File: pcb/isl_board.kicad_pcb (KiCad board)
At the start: 2 copper layers, 82.3 x 75 mm, 98 parts, among them J1 CONN_02X20, J2 SMA_PCLK, J3 SMA_PCLK_SI, J4 SCART-F, J5 CONN_01X02, U1 AP7351C, U2 TLV70033DDC, U3 NCP703SN18T1G, U4 TLV70018, U5 ISL51002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

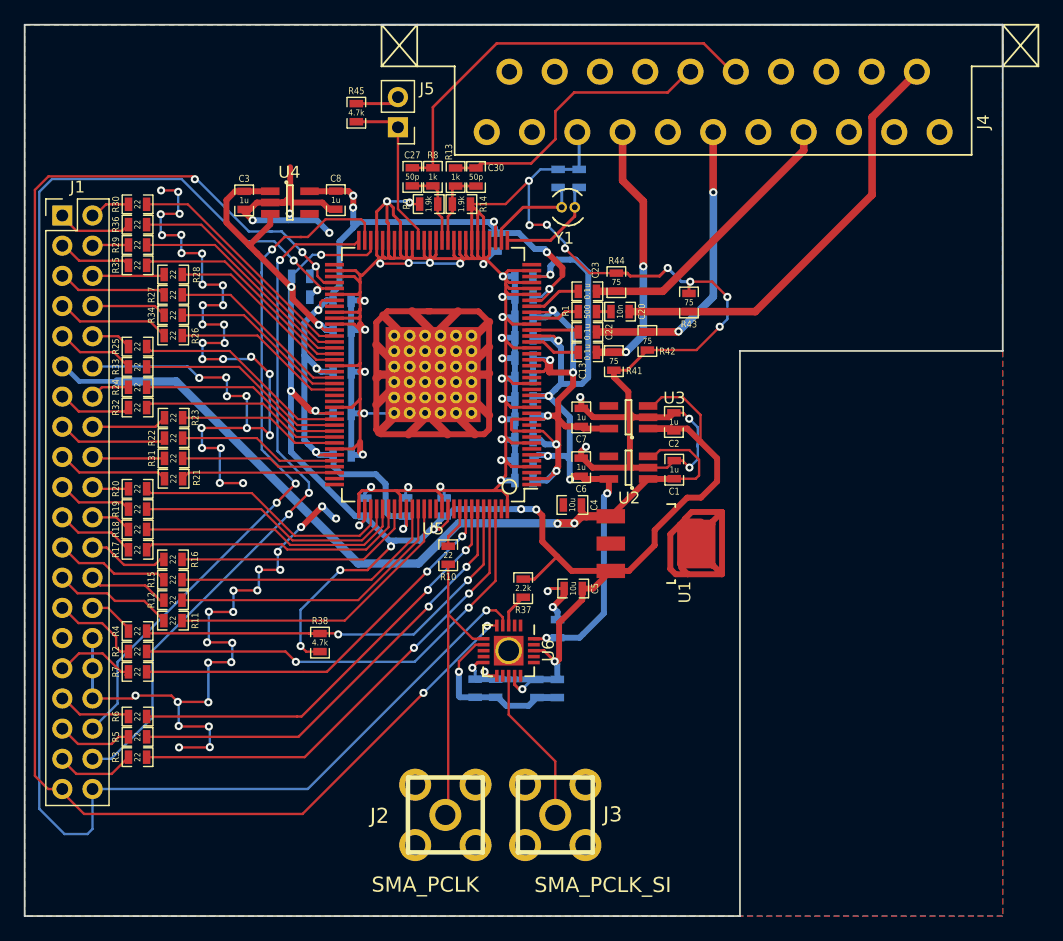
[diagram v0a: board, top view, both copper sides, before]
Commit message: update PCB to v1.1
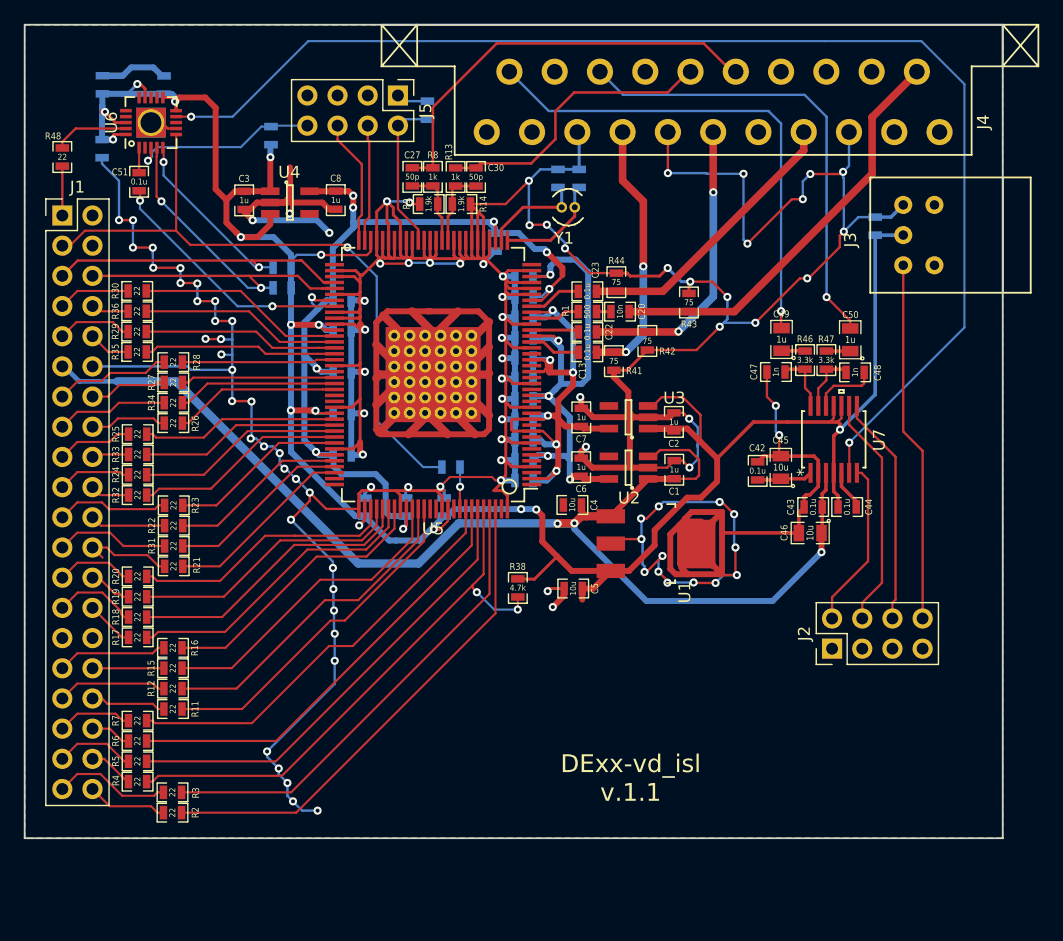
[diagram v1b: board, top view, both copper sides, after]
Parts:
- removed C39, C40: 0.1u, custom_components:SM0603_Capa_libcms
- added C42: 0.1u, custom_components:SM0603_Capa_libcms, F.Cu at (79.1, 64.1)
- added C43: 0.1u, custom_components:SM0603_Capa_libcms, F.Cu at (83.8, 67.1)
- added C44: 0.1u, custom_components:SM0603_Capa_libcms, F.Cu at (86.7, 67.1)
- added C45: 10u, custom_components:SM0805_libcms, F.Cu at (81.1, 63.8)
- added C46: 10u, custom_components:SM0805_libcms, F.Cu at (83.6, 69.3)
- added C47: 1n, custom_components:SM0603_Capa_libcms, F.Cu at (80.7, 55.8)
- added C48: 1n, custom_components:SM0603_Capa_libcms, F.Cu at (87.3, 55.8)
- added C49: 1u, custom_components:SM0805_libcms, F.Cu at (81.2, 53.0)
- added C50: 1u, custom_components:SM0805_libcms, F.Cu at (86.9, 53.1)
- added C51: 0.1u, custom_components:SM0603_Capa_libcms, F.Cu at (27.1, 39.8)
- added C52: 0.1u, custom_components:SM0603_Capa_libcms, B.Cu at (89.0, 43.5)
- added R46: 3.3k, custom_components:SM0603_Resistor_libcms, F.Cu at (83.1, 54.8)
- added R47: 3.3k, custom_components:SM0603_Resistor_libcms, F.Cu at (84.9, 54.8)
- added R48: 22, custom_components:SM0603_Resistor_libcms, F.Cu at (20.6, 37.7)
- added U7: PCM1808PWR, custom_components:PCM1808PWR, F.Cu at (85.5, 61.4)
- J2: value SMA_PCLK -> CONN_AUD; footprint custom_components:SMA_CONN -> Connector_PinHeader_2.54mm:PinHeader_2x04_P2.54mm_Vertical
- J3: value SMA_PCLK_SI -> EAPLRAA4; footprint custom_components:SMA_CONN -> custom_components:EAPLRAA4
- J5: value CONN_01X02 -> CONN_02X04; footprint Pin_Headers:Pin_Header_Straight_1x02_Pitch2.54mm -> Connector_PinHeader_2.54mm:PinHeader_2x04_P2.54mm_Vertical
- R10, R37, R45: moved to B.Cu
- moved C38 63.6 mm to (24.0, 31.6), turned to 90 degrees
- moved C41 57.9 mm to (29.2, 31.6), turned to 90 degrees
- moved J3 56.9 mm to (91.4, 44.2), turned to 270 degrees
- moved C37 55.7 mm to (24.0, 37.0), turned to 270 degrees
- moved U6 53.7 mm to (28.1, 34.8), turned to 90 degrees
- moved R37 43.6 mm to (38.2, 35.9), turned to 270 degrees
- moved J2 35.4 mm to (85.4, 79.0), turned to 90 degrees
- moved R38 17.3 mm to (59.0, 73.9), turned to 90 degrees
- moved R2 13.9 mm to (29.9, 92.8)
- moved R4 12.7 mm to (27.0, 90.2)
- moved R11 7.44 mm to (29.9, 84.1)
- moved R12 7.44 mm to (29.9, 82.4)
- moved R15 7.44 mm to (29.9, 80.7)
- moved R16 7.44 mm to (29.9, 79.0)
- moved R10 7.42 mm to (53.3, 63.8), turned to 0 degrees
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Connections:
- C37 pad 1: /AVCC3v3 -> /DVDD3v3
- J1 pad 1: /B[6] -> /PCLK_SI
- J1 pad 10: /G[7] -> /B[4]
- J1 pad 13: /G[4] -> /B[3]
- J1 pad 14: /G[5] -> /B[2]
- J1 pad 15: /G[2] -> /B[1]
- J1 pad 16: /G[3] -> /B[0]
- J1 pad 17: /G[0] -> /G[7]
- J1 pad 18: /G[1] -> /G[6]
- J1 pad 19: /R[6] -> /G[5]
- J1 pad 2: /B[7] -> GND
- J1 pad 20: /R[7] -> /G[4]
- J1 pad 21: /R[4] -> /G[3]
- J1 pad 22: /R[5] -> /G[2]
- J1 pad 23: /R[2] -> /G[1]
- J1 pad 24: /R[3] -> /G[0]
- J1 pad 25: /R[0] -> /R[7]
- J1 pad 26: /R[1] -> /R[6]
- J1 pad 27: /FID -> /R[5]
- J1 pad 28: /INT_N -> /R[4]
- J1 pad 3: /B[4] -> /PCLK
- J1 pad 31: /HS -> /R[3]
- J1 pad 32: GND -> /R[2]
- J1 pad 33: /HSYNC -> /R[1]
- J1 pad 34: GND -> /R[0]
- J1 pad 35: /VSYNC -> /HS
- J1 pad 36: /CLAMP -> /HSYNC
- J1 pad 37: /DE -> /VSYNC
- J1 pad 38: /COAST -> /INT_N
- J1 pad 39: /SDA -> /DE
- J1 pad 4: /B[5] -> GND
- J1 pad 40: /SCL -> /FID
- J1 pad 5: /B[2] -> /SDA
- J1 pad 6: /B[3] -> /SCL
- J1 pad 7: /B[0] -> /B[7]
- J1 pad 8: /B[1] -> /B[6]
- J1 pad 9: /G[6] -> /B[5]
- J2 pad 1: /PCLK -> GND
- J2 pad 2: GND -> /I2S_WS
- J3 pad 1: /PCLK_SI -> GND
- J3 pad 2: GND -> /DVDD3v3
- J4 pad 2: Net-(J4-Pad2) -> /AUD_R
- J4 pad 6: Net-(J4-Pad6) -> /AUD_L
- J5 pad 1: Net-(J5-Pad1) -> GND
- J5 pad 2: GND -> Net-(J5-Pad2)
- R37 pad 1: /INTR -> /SI_INT_N
- R45 pad 2: Net-(J5-Pad1) -> Net-(J5-Pad2)
- U2 pad 4: (no net) -> Net-(U2-Pad4)
- U3 pad 4: (no net) -> Net-(U3-Pad4)
- U4 pad 4: (no net) -> Net-(U4-Pad4)
- U5 pad 54: Net-(J5-Pad1) -> Net-(J5-Pad2)
- U6 pad 13: /PCLK_SI -> Net-(U6-Pad13)
- U6 pad 20: /AVCC3v3 -> /DVDD3v3
- U6 pad 3: /INTR -> /SI_INT_N
- U6 pad 9: Net-(U6-Pad9) -> /PCM_MCLK
- U6 pad EP: (no net) -> GND
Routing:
- net /PCM_MCLK: track 0.00 -> 107.2 mm, vias 0 -> 2
- net /SCL: track 133.5 -> 40.2 mm, vias 3 -> 2
- net GND: track 637.2 -> 727.2 mm, vias 96 -> 102
- net /SDA: track 128.5 -> 41.0 mm, vias 5 -> 2
- net /CLAMP: track 59.6 -> 9.86 mm, vias 3 -> 0
- net /COAST: track 58.9 -> 10.6 mm, vias 3 -> 0
- net /AUD_R: track 0.00 -> 41.9 mm, vias 0 -> 1
- net /DVDD3v3: track 177.0 -> 218.2 mm
- net /AUD_L: track 0.00 -> 39.3 mm, vias 0 -> 1
- net /DVDD5: track 72.3 -> 104.6 mm, vias 2 -> 3
- net /PCLK: track 25.2 -> 56.1 mm, vias 0 -> 1
- net /SPDIF: track 0.00 -> 30.4 mm
- net Net-(C51-Pad1): track 0.00 -> 21.3 mm, vias 0 -> 2
- net /I2S_DATA: track 0.00 -> 19.7 mm
- net /I2S_BCK: track 0.00 -> 19.3 mm
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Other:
- board size 82.3 x 75 mm -> 82.3 x 68.5 mm
- rule pad_to_mask_clearance: 0.2 -> 0.0508
- board text added: "DExx-vd_isl v.1.1"

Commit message: update PCB to v1.2
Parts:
- added C39: 0.1u, custom_components:SM0603_Capa_libcms, F.Cu at (83.9, 90.9)
- added C53: 0.1u, custom_components:SM0603_Capa_libcms, B.Cu at (32.5, 30.4)
- added DS1: NHD-0220CW-AW3, Connector_PinHeader_2.54mm:PinHeader_1x20_P2.54mm_Vertical, F.Cu at (87.6, 93.7)
- added R49: 10k, custom_components:SM0603_Resistor_libcms, F.Cu at (49.5, 90.4)
- added R50: 10k, custom_components:SM0603_Resistor_libcms, F.Cu at (44.4, 90.4)
- added R51: 1k, custom_components:SM0603_Resistor_libcms, F.Cu at (25.1, 39.8)
- added U8: TSOP31338, OptoDevice:Vishay_CAST-3Pin, F.Cu at (31.3, 28.2)
- C13, C22, C23: value 0.1u -> 1n
- R3: value 22 -> 2.2k
- Y1: value 27MHz -> 24.576MHz
- moved R3 49.1 mm to (26.5, 42.1), turned to 180 degrees
- moved J2 5.83 mm to (79.9, 77.0)
- moved C52 2.48 mm to (89.0, 46.0)
- moved R2 1.67 mm to (29.9, 91.2)
- moved R38 1.57 mm to (59.1, 72.4)
- moved R45 1.11 mm to (52.5, 33.7)
- moved J5 1.03 mm to (49.9, 32.5)
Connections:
- J1 pad 39: /DE -> /IR_RX
- J3 pad 1: GND -> /SPDIF
- J3 pad 2: /DVDD3v3 -> GND
- J3 pad 3: /SPDIF -> /DVDD3v3
- R3 pad 1: /DE -> /CLK24P576
- R3 pad 2: Net-(R3-Pad2) -> Net-(C51-Pad1)
- U5 pad 125: Net-(R3-Pad2) -> Net-(U5-Pad125)
- U5 pad 72: Net-(C51-Pad1) -> /CLK24P576
- U6 pad 9: /PCM_MCLK -> Net-(U6-Pad9)
- U7 pad 6: /PCM_MCLK -> /CLK24P576
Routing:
- net /CLK24P576: track 0.00 -> 133.2 mm, vias 0 -> 3
- net /PCM_MCLK: track 107.2 -> 0.00 mm, vias 2 -> 0
- net /DVDD3v3: track 218.2 -> 320.9 mm, vias 16 -> 18
- net /SCL: track 40.2 -> 122.1 mm
- net /SDA: track 41.0 -> 121.6 mm
- net /IR_RX: track 0.00 -> 80.4 mm
- net GND: track 727.2 -> 798.2 mm, vias 102 -> 105
- net Net-(R3-Pad2): track 40.0 -> 0.00 mm
- net Net-(C51-Pad1): track 21.3 -> 3.70 mm, vias 2 -> 0
- net /DE: track 9.91 -> 0.00 mm
- net /SPDIF: track 30.4 -> 35.0 mm
- net /SI_INT_N: track 16.0 -> 19.4 mm, vias 1 -> 2
- net Net-(DS1-Pad18): track 0.00 -> 2.55 mm
- net Net-(DS1-Pad16): track 0.00 -> 2.53 mm
- net Net-(R2-Pad2): track 42.2 -> 40.0 mm
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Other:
- outline, holes or cut-outs redrawn
- board text added: "DExx-vd_isl v.1.2"
- board text removed: "DExx-vd_isl v.1.1"

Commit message: update PCB to v1.3
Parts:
- added L1: 2.2u, custom_components:CDRH2D14, F.Cu at (70.2, 71.1)
- added SW1: SW_SPDT, Connector_PinHeader_2.54mm:PinHeader_1x03_P2.54mm_Vertical, F.Cu at (76.6, 53.2)
- R10: value 22 -> 50; moved to F.Cu
- R48: value 22 -> 50
- U1: value AP7351C -> LM3671MF-2.5/NOPB; footprint custom_components:SOT-223_Handsoldering -> custom_components:SOT-23-5_Handsoldering
- U2: value TLV70033DDC -> TLV70033
- U3: value NCP703SN18T1G -> TLV75518P
- U4: value TLV70018 -> TLV75518P
- Y1: value 24.576MHz -> 27MHz
- moved U8 68.8 mm to (18.9, 95.9)
- moved C53 66.9 mm to (23.9, 96.7), turned to 270 degrees
- moved C3 41.6 mm to (62.4, 73.4), turned to 90 degrees
- moved U4 36.8 mm to (58.6, 73.2), turned to 90 degrees
- moved C8 33.9 mm to (54.7, 73.4), turned to 90 degrees
- moved R38 31.4 mm to (35.6, 93.3), turned to 270 degrees
- moved R10 24.5 mm to (39.1, 43.9)
- moved C4 13.8 mm to (69.5, 79.5), turned to 0 degrees
- moved C5 11.2 mm to (73.6, 68.8), turned to 0 degrees
- moved R43 6.36 mm to (79.6, 48.8), turned to 0 degrees
- moved U1 5.72 mm to (70.2, 75.9), turned to 0 degrees
- moved C1 5.10 mm to (72.1, 58.9)
- moved C6 5.10 mm to (64.3, 58.7)
- moved U2 5.10 mm to (68.2, 58.7)
- moved C2 4.65 mm to (72.1, 64.6)
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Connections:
- C2 pad 1: /DVDD3v3 -> /DVDD2v5
- C20 pad 1: /SOG_in -> /SOG
- C3 pad 1: /DVDD3v3 -> /DVDD2v5
- C5 pad 1: /DVDD3v3 -> /DVDD2v5
- J1 pad 2: GND -> /PCLK
- J1 pad 29: Net-(J1-Pad29) -> /DVDD3v3
- J1 pad 3: /PCLK -> GND
- J4 pad 20: /SOG_in -> /SYNC_in
- R3 pad 1: /CLK24P576 -> /CLK27
- R43 pad 1: /SOG_in -> /SYNC_in
- U1 pad 3: /DVDD3v3 -> /DVDD5
- U2 pad 4: Net-(U2-Pad4) -> GND
- U3 pad 1: /DVDD3v3 -> /DVDD2v5
- U3 pad 3: /DVDD3v3 -> /DVDD2v5
- U3 pad 4: Net-(U3-Pad4) -> GND
- U4 pad 1: /DVDD3v3 -> /DVDD2v5
- U4 pad 3: /DVDD3v3 -> /DVDD2v5
- U4 pad 4: Net-(U4-Pad4) -> GND
- U5 pad 72: /CLK24P576 -> /CLK27
- U6 pad 9: Net-(U6-Pad9) -> /PCM_MCLK
- U7 pad 6: /CLK24P576 -> /PCM_MCLK
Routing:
- net GND: track 798.2 -> 425.0 mm, vias 105 -> 338
- net /DVDD3v3: track 320.9 -> 118.8 mm, vias 18 -> 17
- net /CLK24P576: track 133.2 -> 0.00 mm, vias 3 -> 0
- net /PCM_MCLK: track 0.00 -> 109.9 mm, vias 0 -> 2
- net /IR_RX: track 80.4 -> 8.00 mm
- net /SOG_in: track 40.5 -> 0.00 mm
- net Net-(R10-Pad2): track 3.52 -> 34.1 mm, vias 1 -> 0
- net /SYNC_in: track 0.00 -> 30.0 mm
- net /PCLK: track 56.1 -> 26.9 mm, vias 1 -> 0
- net /DVDD5: track 104.6 -> 78.5 mm, vias 3 -> 23
- net /DVDD2v5: track 0.00 -> 24.5 mm, vias 0 -> 11
- net /CLK27: track 0.00 -> 19.7 mm, vias 0 -> 2
- net /DVDD1v8: track 84.7 -> 66.4 mm, vias 9 -> 14
- net /SCL: track 122.1 -> 108.9 mm, vias 2 -> 3
- net /SOG: track 0.00 -> 8.32 mm
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- added copper zone on F.Cu, net /AVCC1v8
- added copper zone on In2.Cu, net /AVCC3v3
- added copper zone on In2.Cu, net /DVDD1v8
- added copper zone on In2.Cu, net /DVDD2v5
- added copper zone on In2.Cu, net /DVDD3v3
- added copper zone on In2.Cu, net /DVDD5
- added copper zone on In1.Cu, net GND
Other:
- board size 82.3 x 68.5 mm -> 82.3 x 71.9 mm
- copper layers 2 -> 4
- board text added: "CSYNC"
- board text added: "DExx-vd_isl v.1.3"
- board text added: "SOG"
- board text removed: "DExx-vd_isl v.1.2"

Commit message: update PCB to v1.4
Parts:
- added JP1: SolderJumper_2_Open, custom_components:SolderJumper-2_P1.3mm_Open_Pad1.0x0.75mm, F.Cu at (22.2, 37.6)
- J3: value EAPLRAA4 -> FCR684208R; footprint custom_components:EAPLRAA4 -> custom_components:FCR684208R
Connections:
- J1 pad 2: /PCLK -> unconnected-(J1-Pad2)
- J1 pad 3: GND -> /PCLK
- J1 pad 4: GND -> unconnected-(J1-Pad4)
- J3 pad 4: Net-(J3-Pad4) -> unconnected-(J3-Pad4)
- J3 pad 5: Net-(J3-Pad5) -> unconnected-(J3-Pad5)
- J4 pad 1: Net-(J4-Pad1) -> unconnected-(J4-Pad1)
- J4 pad 16: Net-(J4-Pad16) -> unconnected-(J4-Pad16)
- J4 pad 19: Net-(J4-Pad19) -> unconnected-(J4-Pad19)
- J4 pad 3: Net-(J4-Pad3) -> unconnected-(J4-Pad3)
- J4 pad 8: Net-(J4-Pad8) -> unconnected-(J4-Pad8)
- R10 pad 2: Net-(R10-Pad2) -> /C1
- U2 pad 4: GND -> unconnected-(U2-Pad4)
- U3 pad 4: GND -> unconnected-(U3-Pad4)
- U4 pad 4: GND -> unconnected-(U4-Pad4)
- U5 pad 1: Net-(U5-Pad1) -> unconnected-(U5-Pad1)
- U5 pad 101: Net-(U5-Pad101) -> unconnected-(U5-Pad101)
- U5 pad 102: Net-(U5-Pad102) -> unconnected-(U5-Pad102)
- U5 pad 11: Net-(U5-Pad11) -> unconnected-(U5-Pad11)
- U5 pad 115: Net-(U5-Pad115) -> unconnected-(U5-Pad115)
- U5 pad 116: Net-(U5-Pad116) -> unconnected-(U5-Pad116)
- U5 pad 119: Net-(U5-Pad119) -> unconnected-(U5-Pad119)
- U5 pad 120: Net-(R10-Pad2) -> /C1
- U5 pad 125: Net-(U5-Pad125) -> unconnected-(U5-Pad125)
- U5 pad 127: Net-(U5-Pad127) -> unconnected-(U5-Pad127)
- U5 pad 13: Net-(U5-Pad13) -> unconnected-(U5-Pad13)
- U5 pad 15: Net-(U5-Pad15) -> unconnected-(U5-Pad15)
- U5 pad 17: Net-(U5-Pad17) -> unconnected-(U5-Pad17)
- U5 pad 19: Net-(U5-Pad19) -> unconnected-(U5-Pad19)
- U5 pad 21: Net-(U5-Pad21) -> unconnected-(U5-Pad21)
- U5 pad 23: Net-(U5-Pad23) -> unconnected-(U5-Pad23)
- U5 pad 3: Net-(U5-Pad3) -> unconnected-(U5-Pad3)
- U5 pad 38: Net-(U5-Pad38) -> unconnected-(U5-Pad38)
- U5 pad 5: Net-(U5-Pad5) -> unconnected-(U5-Pad5)
- U5 pad 65: Net-(U5-Pad65) -> unconnected-(U5-Pad65)
- U5 pad 7: Net-(U5-Pad7) -> unconnected-(U5-Pad7)
- U5 pad 87: Net-(U5-Pad87) -> unconnected-(U5-Pad87)
- U5 pad 88: Net-(U5-Pad88) -> unconnected-(U5-Pad88)
- U5 pad 9: Net-(U5-Pad9) -> unconnected-(U5-Pad9)
- U6 pad 12: Net-(U6-Pad12) -> unconnected-(U6-Pad12)
- U6 pad 13: Net-(U6-Pad13) -> unconnected-(U6-Pad13)
- U6 pad 15: Net-(U6-Pad15) -> unconnected-(U6-Pad15)
- U6 pad 16: Net-(U6-Pad16) -> unconnected-(U6-Pad16)
- U6 pad 17: Net-(U6-Pad17) -> unconnected-(U6-Pad17)
- U6 pad 2: Net-(U6-Pad2) -> unconnected-(U6-Pad2)
- U6 pad 6: /PCLK -> /C1
- U6 pad 8: Net-(U6-Pad8) -> unconnected-(U6-Pad8)
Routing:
- net /C1: track 0.00 -> 47.4 mm
- net Net-(R10-Pad2): track 34.1 -> 0.00 mm
- net /PCLK: track 26.9 -> 18.7 mm
- net GND: track 425.0 -> 417.9 mm, vias 338 -> 332
- net /SDA: track 116.2 -> 114.4 mm
- net /B_in: track 24.0 -> 22.3 mm
- net /AVCC3v3: track 47.3 -> 45.7 mm
- net Net-(JP1-Pad1): track 6.33 -> 7.89 mm
- net /PCLK_SI: track 3.90 -> 5.39 mm
- net /DVDD3v3: track 118.8 -> 117.5 mm
- net /G[0]: track 7.92 -> 6.72 mm
- net /SCL: track 108.9 -> 107.8 mm
- net /PCM_MCLK: track 109.9 -> 110.8 mm
- net /DVDD1v8: track 66.4 -> 65.8 mm
- net /B[4]: track 4.08 -> 3.54 mm
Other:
- net class 75ohm_vid removed
- net class Default removed
- net class Power removed
- net class digi_hs removed
- board text added: "DExx-vd_isl v.1.4"
- board text removed: "DExx-vd_isl v.1.3"
